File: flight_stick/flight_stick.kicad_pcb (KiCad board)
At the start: 2 copper layers, 96 x 96 mm, 80 parts, among them J1 Load Cell 1, J10 USB_C_Receptacle_USB2.0, J11 Conn_01x05_Pin, J2 Load Cell 2, J3 Load Cell 5, J4 Load Cell 6, J5 Load Cell 3, J6 Load Cell 4, J7 Conn_01x04_Male, J8 Conn_01x05_Pin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

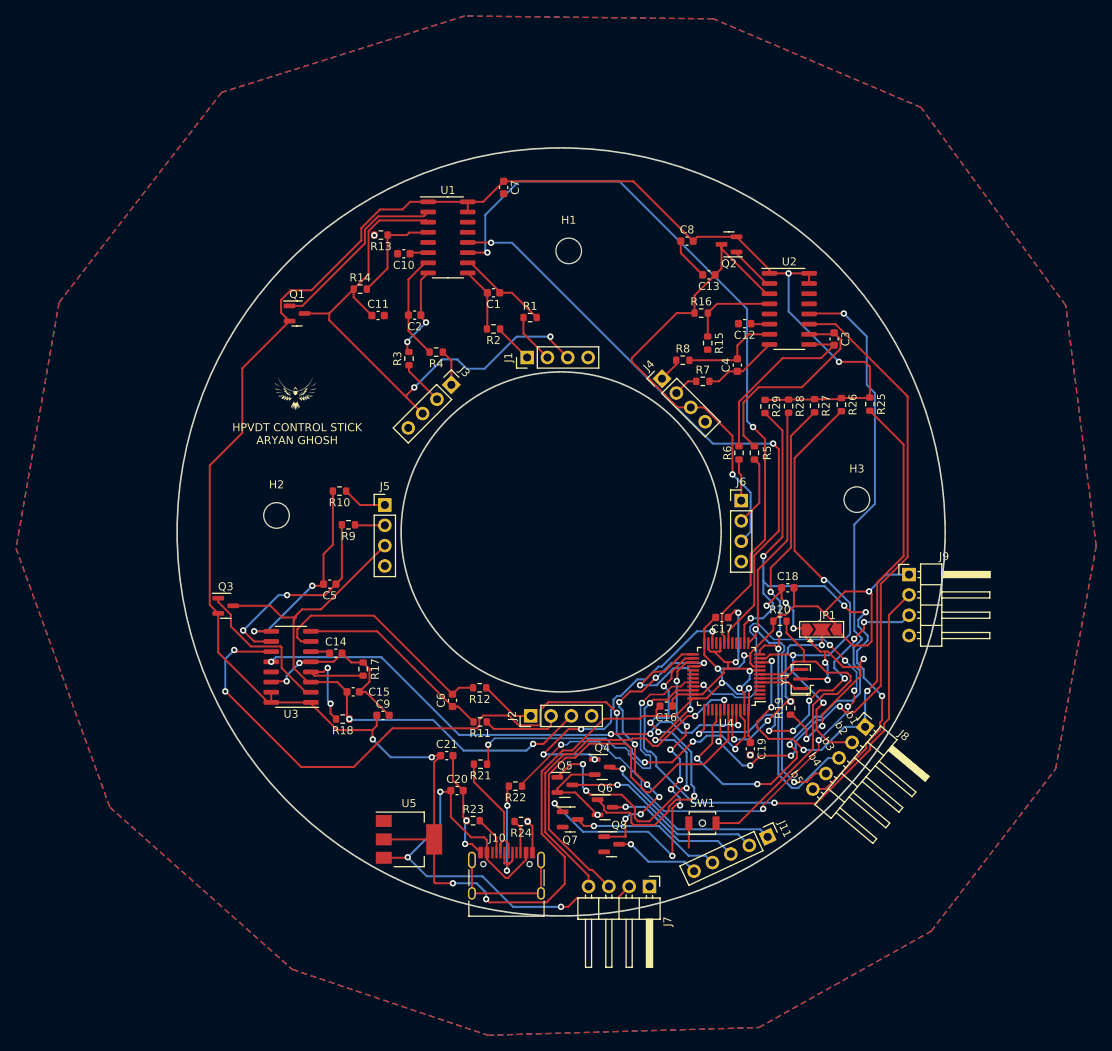
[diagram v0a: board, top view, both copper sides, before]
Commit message: updated 3rd revision
reduced the number of strain gauges and updated the schematic and placed the initial layout without traces.
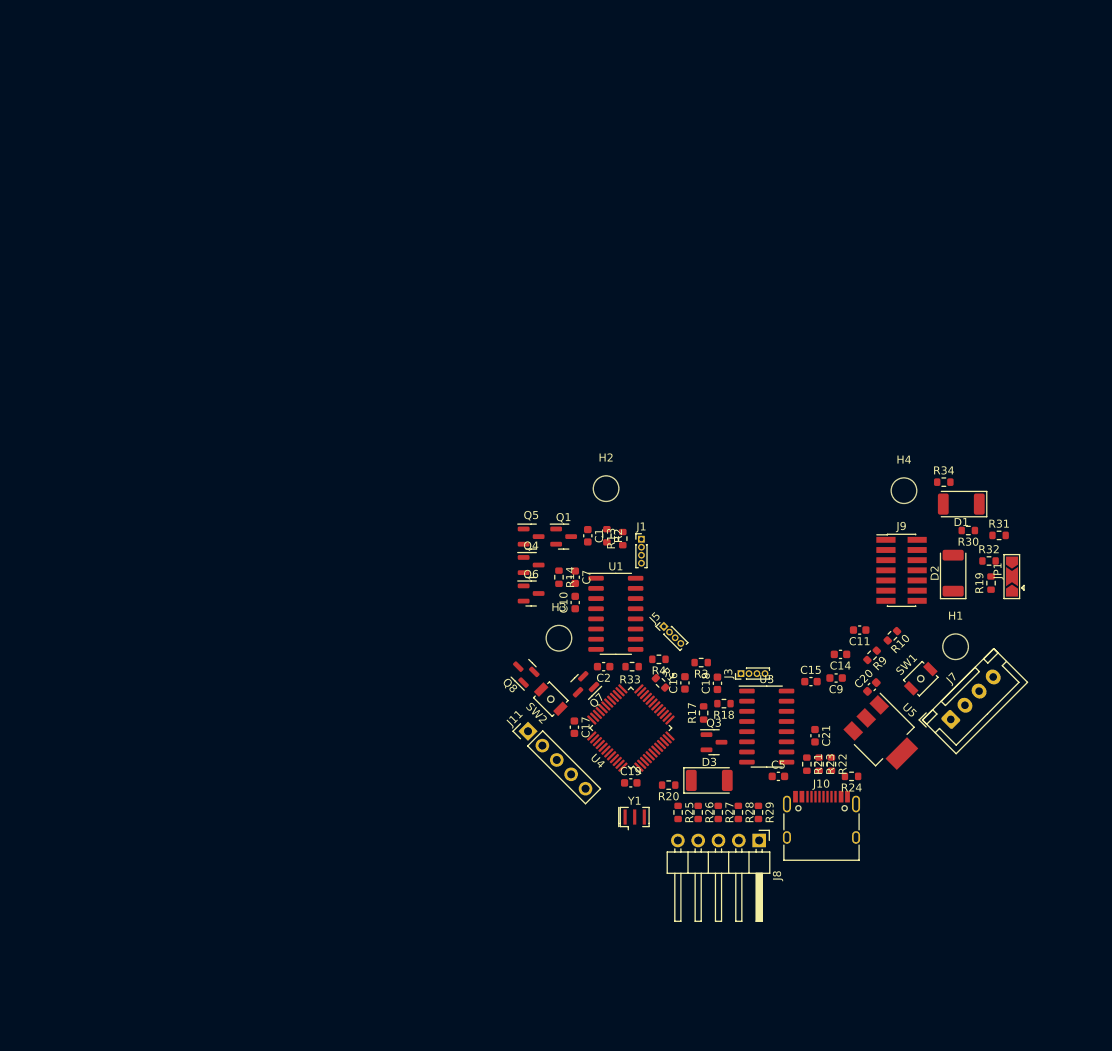
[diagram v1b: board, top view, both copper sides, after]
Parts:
- removed C12, C3, C4, C6: 0.1uF, Capacitor_SMD:C_0603_1608Metric
- removed C13, C8: 10uF, Capacitor_SMD:C_0603_1608Metric
- removed J2: Load Cell 2, Connector_PinHeader_2.54mm:PinHeader_1x04_P2.54mm_Vertical
- removed J4: Load Cell 6, Connector_PinHeader_2.54mm:PinHeader_1x04_P2.54mm_Vertical
- removed J6: Load Cell 4, Connector_PinHeader_2.54mm:PinHeader_1x04_P2.54mm_Vertical
- removed Q2: MMS8550, Package_TO_SOT_SMD:SOT-23
- removed R11, R12, R5, R6, R7, R8: 100, Resistor_SMD:R_0603_1608Metric
- removed R15: 8.2k, Resistor_SMD:R_0603_1608Metric
- removed R16: 20k, Resistor_SMD:R_0603_1608Metric
- removed U2: HX711, Package_SO:SOIC-16_3.9x9.9mm_P1.27mm
- added D1: LED, LED_SMD:LED_2010_5025Metric, F.Cu at (160.0, 96.5)
- added D2: LED, LED_SMD:LED_2010_5025Metric, F.Cu at (159.0, 105.2)
- added D3: LED, LED_SMD:LED_2010_5025Metric, F.Cu at (128.5, 131.1)
- added H4: MountingHole, MountingHole:MountingHole_3.2mm_M3_ISO7380, F.Cu at (152.9, 94.8)
- added R30: 50, Resistor_SMD:R_0603_1608Metric, F.Cu at (160.9, 99.8)
- added R31: 30, Resistor_SMD:R_0603_1608Metric, F.Cu at (164.7, 100.4)
- added R32: R_US, Resistor_SMD:R_0603_1608Metric, F.Cu at (163.5, 103.6)
- added R33: R_US, Resistor_SMD:R_0603_1608Metric, F.Cu at (118.9, 116.8)
- added R34: 30, Resistor_SMD:R_0603_1608Metric, F.Cu at (157.8, 93.8)
- added SW2: SW_Push, Button_Switch_SMD:SW_SPST_B3U-1000P-B, F.Cu at (108.7, 120.9)
- C20: value 10uF -> 0.47uF
- C21: value 22uF -> 33uF
- J1, J3, J5: footprint Connector_PinHeader_2.54mm:PinHeader_1x04_P2.54mm_Vertical -> Connector_PinHeader_1.00mm:PinHeader_1x04_P1.00mm_Vertical
- J7: footprint Connector_PinHeader_2.54mm:PinHeader_1x04_P2.54mm_Horizontal -> Connector_JST:JST_XH_B4B-XH-A_1x04_P2.50mm_Vertical
- J9: value Conn_01x04_Male -> Conn_ST_STDC14; footprint Connector_PinHeader_2.54mm:PinHeader_1x04_P2.54mm_Horizontal -> Connector_PinHeader_1.27mm:PinHeader_2x07_P1.27mm_Vertical_SMD
- U5: value AZ1117-3.3 -> LM3940IMP-3.3/NOPB; footprint Package_TO_SOT_SMD:SOT-223-3_TabPin2 -> Package_TO_SOT_SMD:SOT-223
- moved C11 71.9 mm to (147.3, 112.3), turned to 180 degrees
- moved R10 71.4 mm to (151.4, 113.0), turned to -135 degrees
- moved H1 69.2 mm to (159.3, 114.4)
- moved R9 67.5 mm to (148.9, 115.4), turned to -135 degrees
- moved Q3 63.4 mm to (129.1, 126.3)
- moved C14 63.1 mm to (144.9, 115.3), turned to 180 degrees
- moved C5 61.0 mm to (137.2, 130.6), turned to 0 degrees
- moved U5 60.8 mm to (150.4, 125.5), turned to -45 degrees
- moved U3 59.9 mm to (135.7, 124.3), turned to 0 degrees
- moved C15 57.2 mm to (141.2, 118.7)
- moved C9 56.8 mm to (144.4, 118.3), turned to 180 degrees
- moved R25 56.4 mm to (124.6, 135.1)
- moved R26 54.0 mm to (127.1, 135.1)
- moved C20 53.4 mm to (148.8, 119.4), turned to 45 degrees
- moved R3 52.7 mm to (127.5, 116.3), turned to 180 degrees
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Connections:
- J8 pad 1: /button1 -> /button5
- J8 pad 2: /button2 -> /button4
- J8 pad 4: /button4 -> /button2
- J8 pad 5: /button5 -> /button1
- J9 pad 1: +3.3V -> unconnected-(J9-NC-Pad1)
- J9 pad 2: /codeio -> unconnected-(J9-NC-Pad2)
- J9 pad 3: /codeclk -> +3.3V
- J9 pad 4: GND -> /codeio
- R20 pad 2: Net-(U4-NRST) -> /mcureset
- SW1 pad 2: Net-(U4-NRST) -> /mcureset
- U3 pad 7: Net-(U3-IN_{A-}) -> unconnected-(U3-IN_{A-}-Pad7)
- U3 pad 8: Net-(U3-IN_{A+}) -> unconnected-(U3-IN_{A+}-Pad8)
- U4 pad 12: /button3 -> /Programming_{TX}
- U4 pad 13: /button4 -> /Programming_{RX}
- U4 pad 14: /button5 -> /button3
- U4 pad 15: unconnected-(U4-PA5-Pad15) -> /button4
- U4 pad 16: unconnected-(U4-PA6-Pad16) -> /button5
- U4 pad 17: unconnected-(U4-PA7-Pad17) -> Net-(U4-PA7)
- U4 pad 29: unconnected-(U4-PA8-Pad29) -> Net-(U4-PA8)
- U4 pad 7: Net-(U4-NRST) -> /mcureset
- U5 pad 1: GND -> +5V
- U5 pad 2: +3.3V -> GND
- U5 pad 3: +5V -> +3.3V
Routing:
- net +3.3V: track 358.3 -> 0.00 mm, vias 11 -> 0
- net GND: track 144.6 -> 0.00 mm, vias 20 -> 0
- net clk-yforce: track 96.6 -> 0.00 mm, vias 6 -> 0
- net clk-xforce: track 93.4 -> 0.00 mm, vias 2 -> 0
- net /D+: track 92.4 -> 0.00 mm, vias 8 -> 0
- net dout-shear: track 91.5 -> 0.00 mm, vias 4 -> 0
- net clk-shear: track 84.8 -> 0.00 mm, vias 4 -> 0
- net /button5: track 77.2 -> 0.00 mm, vias 5 -> 0
- net dout-xforce: track 76.4 -> 0.00 mm, vias 2 -> 0
- net /E+_{LC3&4}: track 72.6 -> 0.00 mm, vias 2 -> 0
- net /E+_{LC1&2}: track 70.9 -> 0.00 mm, vias 2 -> 0
- net /button1: track 69.8 -> 0.00 mm, vias 4 -> 0
- net /codeio: track 67.9 -> 0.00 mm, vias 2 -> 0
- net dout-yforce: track 66.4 -> 0.00 mm, vias 4 -> 0
- net +5V: track 65.1 -> 0.00 mm, vias 3 -> 0
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- removed copper zone on B.Cu, net GND
- removed copper zone on F.Cu, net GND
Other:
- board outline removed
- board text removed: "HPVDT CONTROL STICK ARYAN GHOSH"
- board text removed: "b1"
- board text removed: "b2"
- board text removed: "b3"
- board text removed: "b4"
- board text removed: "b5"
- board text removed: "locked"

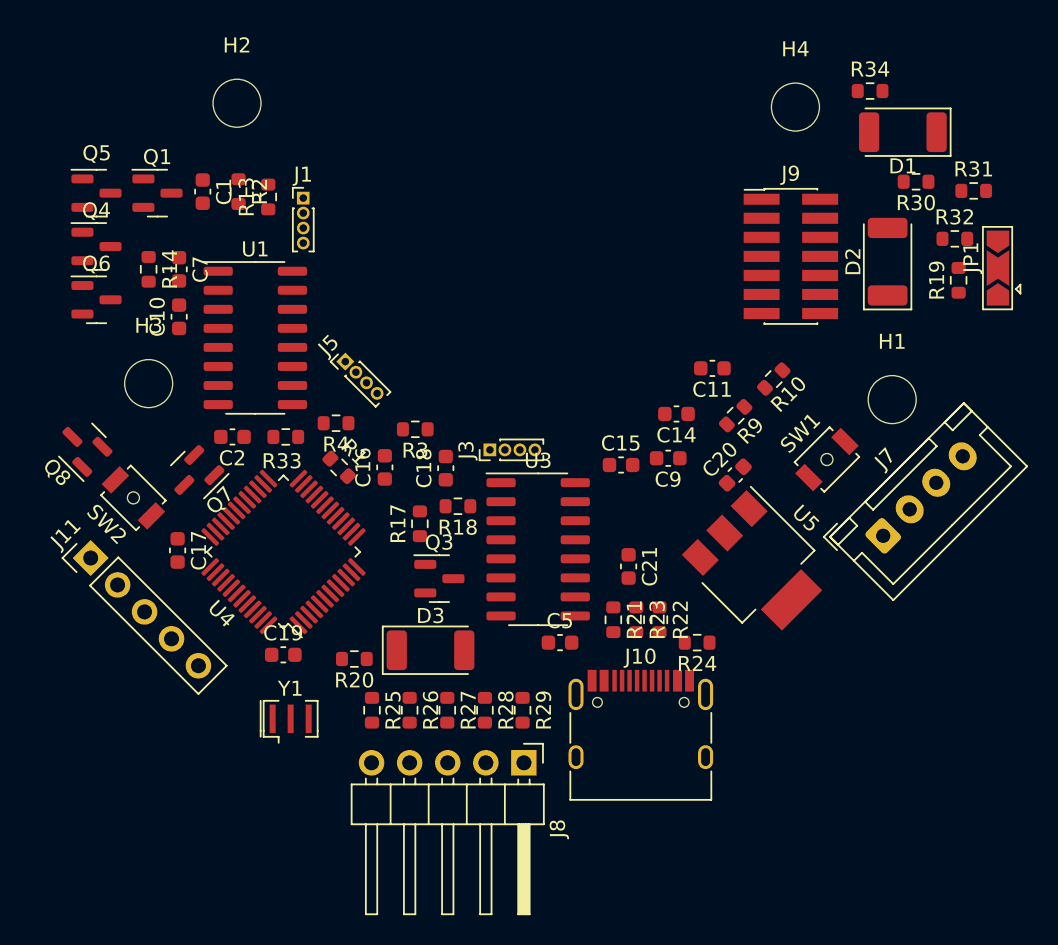
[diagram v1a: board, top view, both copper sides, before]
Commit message: Made Recommended changes
From savo:
C11 is a decoupling capacitor for one of the HX711s, it should be closer to it
You can get rid of two of the mounting holes. Two are enough.
Try to bring the USB stuff closer to the STM32, since it operates at high speed and we should keep the connections short.
Similarly try to bring the programming header closer to the STM32.
You can move the button stuff further from the STM32, those will be operated at kHz which is "slow"
The resistors you picked for the LEDs are a fair bit smaller than needed, 100+ Ohms is good.
No need for the pulldown R34
Power LEDs are cool, but maybe just one on the 3V3 rail is enough since thats the critical line. You can probably use the other one as a user configurable one too
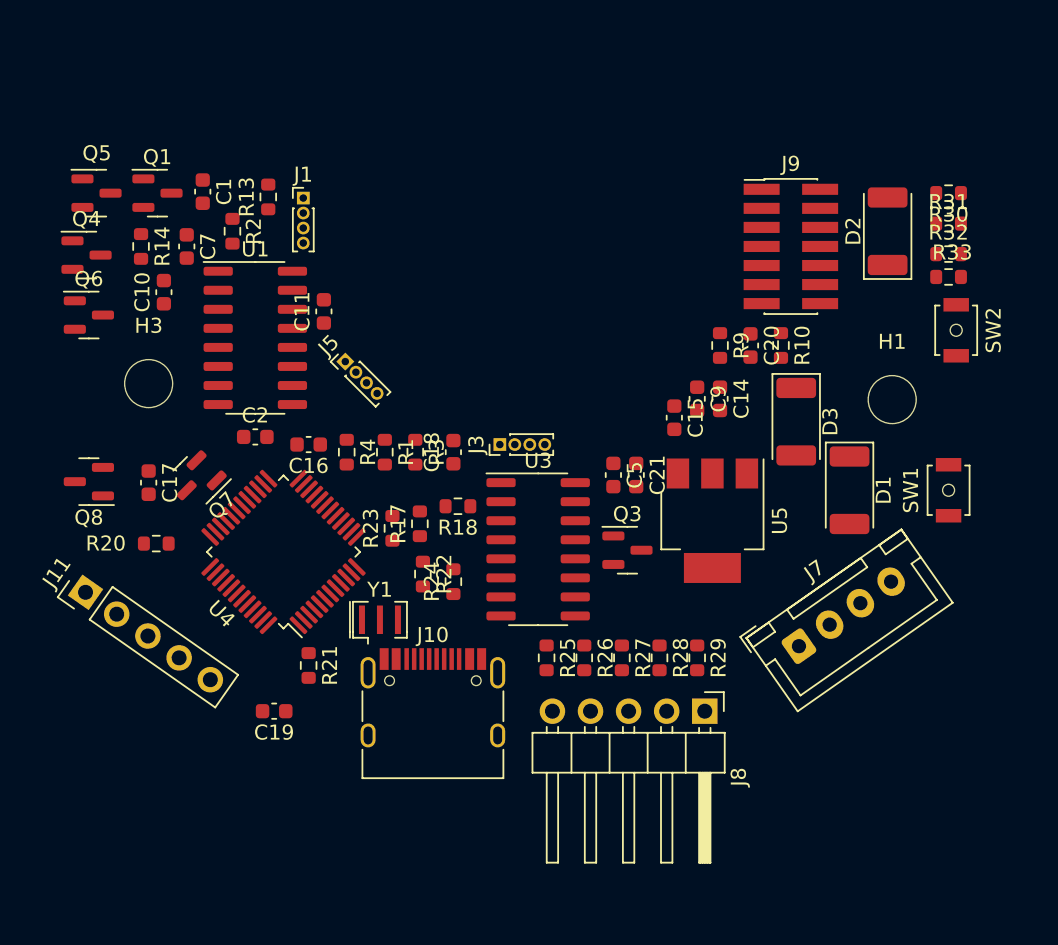
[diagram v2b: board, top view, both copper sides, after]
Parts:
- removed H2, H4: MountingHole, MountingHole:MountingHole_3.2mm_M3_ISO7380
- removed JP1: Jumper_3_Open, Jumper:SolderJumper-3_P2.0mm_Open_TrianglePad1.0x1.5mm
- removed R19: 10k, Resistor_SMD:R_0603_1608Metric
- removed R34: 30, Resistor_SMD:R_0603_1608Metric
- moved SW2 56.0 mm to (163.6, 109.7), turned to -90 degrees
- moved R33 45.5 mm to (163.1, 106.2), turned to 180 degrees
- moved D3 28.8 mm to (152.9, 115.8), turned to -90 degrees
- moved C11 26.2 mm to (121.4, 108.5), turned to 90 degrees
- moved D1 24.1 mm to (156.5, 120.4), turned to -90 degrees
- moved R21 20.5 mm to (120.4, 132.1)
- moved R23 17.4 mm to (126.0, 122.9), turned to 90 degrees
- moved R24 16.8 mm to (130.0, 126.5), turned to 90 degrees
- moved R22 16.1 mm to (128.0, 126.0)
- moved R20 15.3 mm to (110.2, 124.0), turned to 0 degrees
- moved J10 13.9 mm to (128.7, 135.7)
- moved Q3 12.7 mm to (141.7, 124.4)
- moved J8 12.5 mm to (146.8, 135.1)
- moved R25 12.2 mm to (136.3, 131.6)
- moved R28 12.2 mm to (143.8, 131.6)
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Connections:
- U4 pad 44: Net-(JP1-C) -> GND

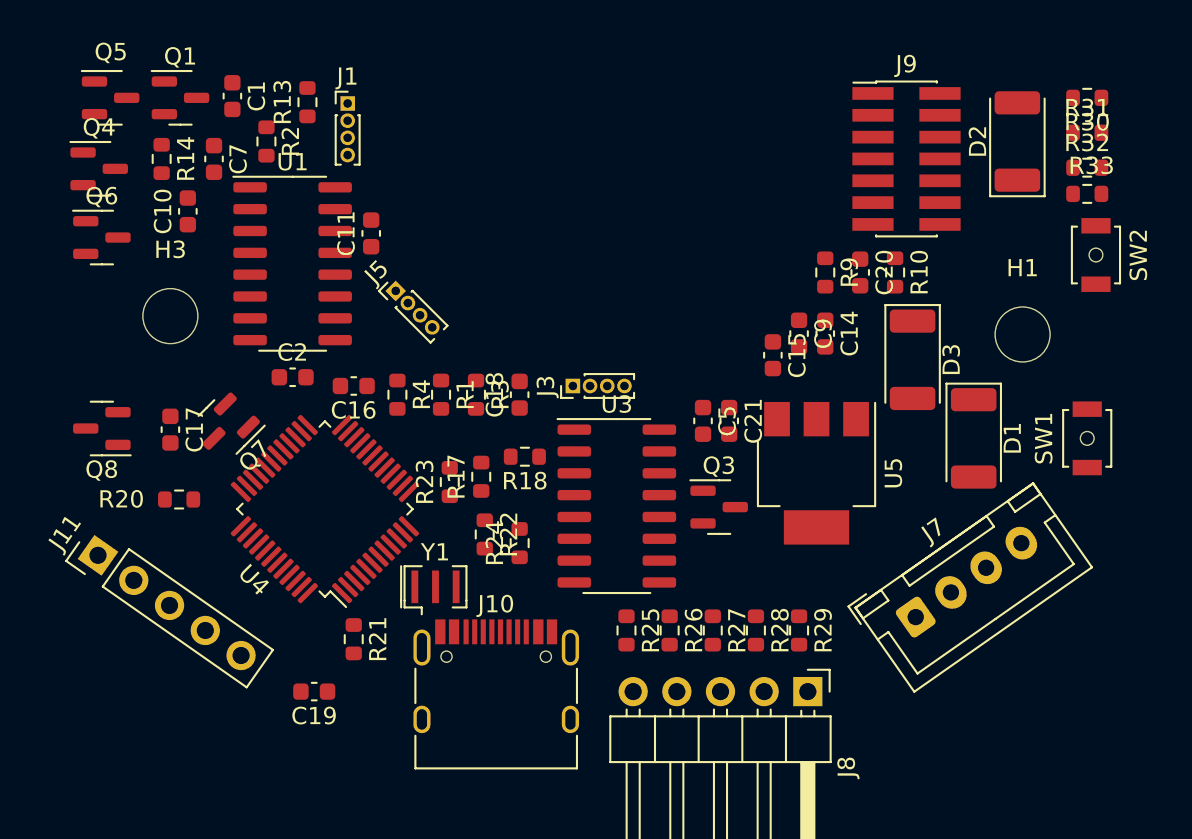
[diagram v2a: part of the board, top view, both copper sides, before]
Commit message: Updated Layout
Board is now symetrical and necessary components are locked
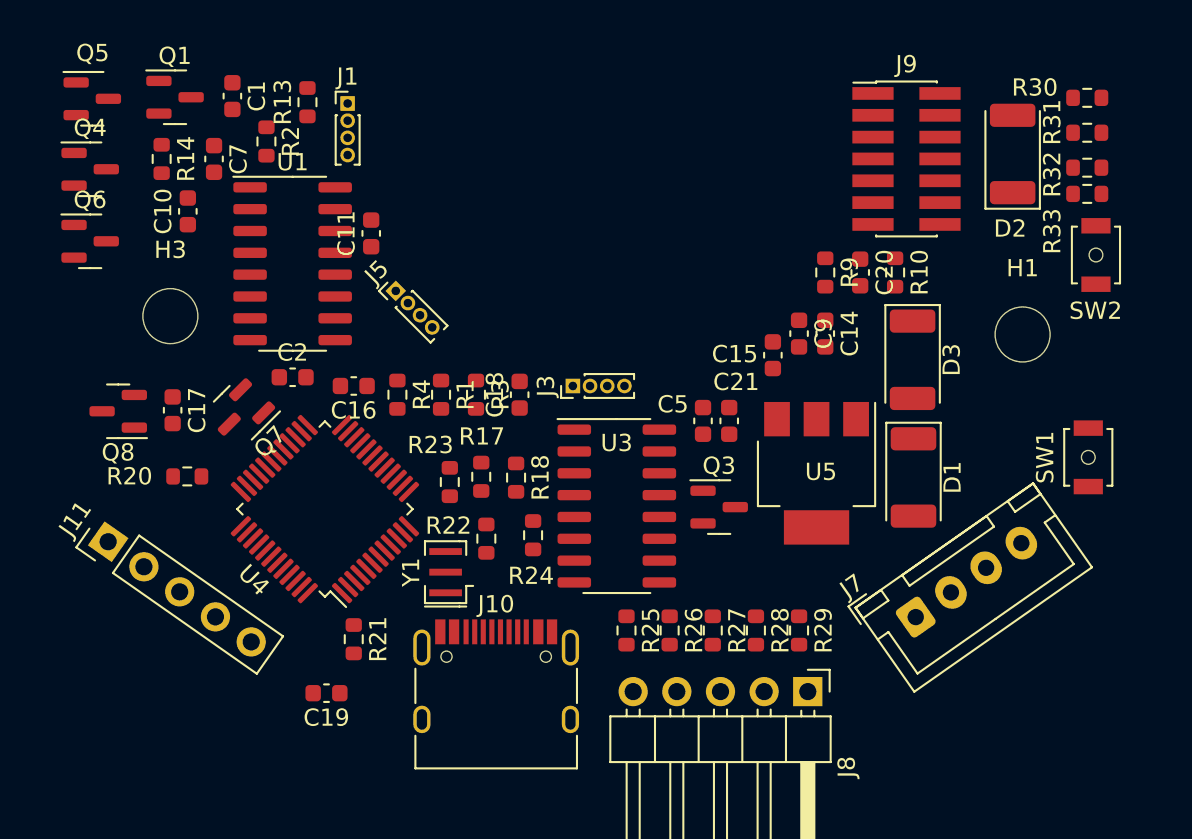
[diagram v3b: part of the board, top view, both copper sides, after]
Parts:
- R30: value 50 -> 130
- R31: value 30 -> 100
- moved D1 4.18 mm to (153.0, 122.7)
- moved R20 1.42 mm to (110.7, 122.6)
- moved Q8 1.38 mm to (106.7, 118.8)
- moved R18 1.32 mm to (129.8, 122.7), turned to -90 degrees
- moved Q7 1.21 mm to (113.8, 118.9)
- moved C17 1.14 mm to (109.9, 118.8)
- moved SW1 1.11 mm to (163.1, 121.5)
- moved Q5 1.07 mm to (105.2, 100.6)
- moved Y1 1.04 mm to (125.7, 128.2), turned to 90 degrees
- moved J11 0.99 mm to (106.1, 126.4)
- moved R24 0.91 mm to (130.8, 126.0)
- moved D2 0.78 mm to (158.7, 103.8)
- moved C19 0.72 mm to (118.8, 135.2)
- moved Q6 0.72 mm to (105.1, 108.9)
- moved Q4 0.52 mm to (105.1, 104.7)
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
